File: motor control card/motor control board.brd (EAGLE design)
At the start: 100 x 80 mm, 13 parts, among them J1 8-1393644-0, J2 TBP02R1-381-07BE, J3 TBP02R1-381-07BE

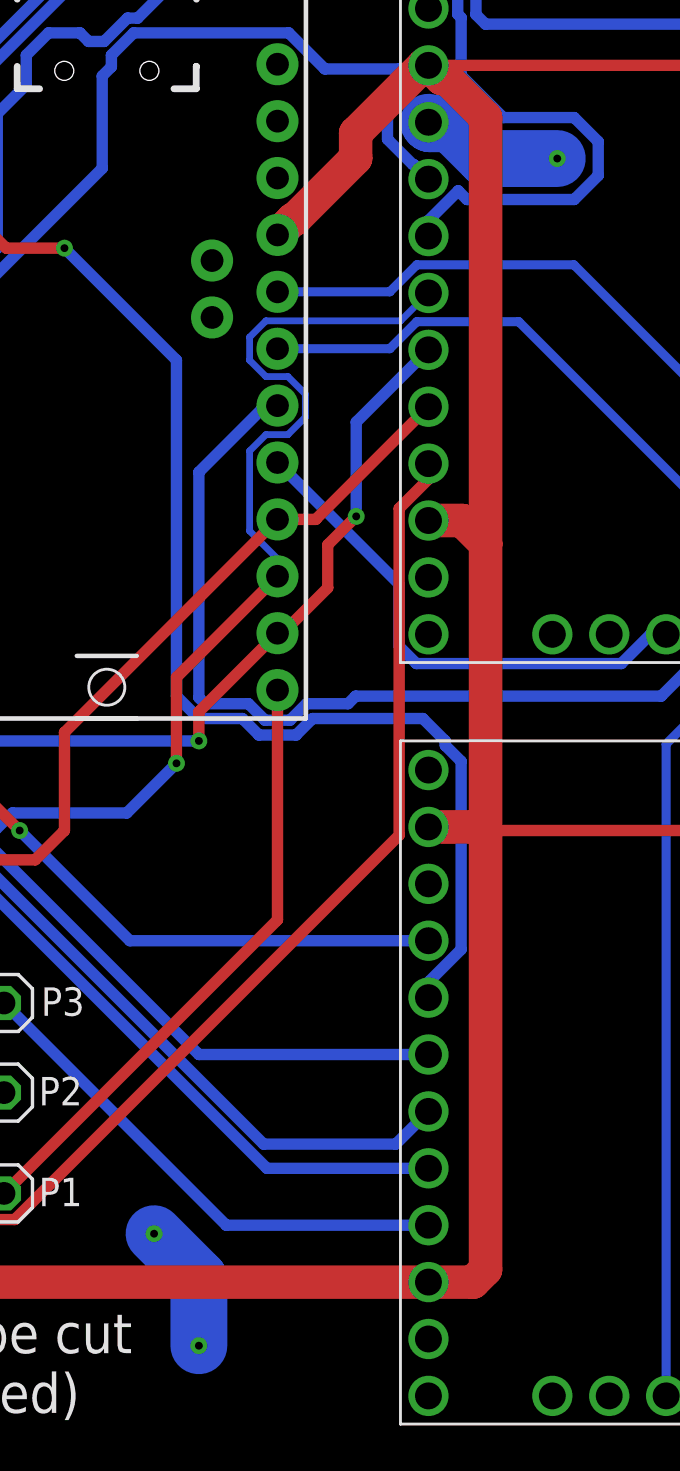
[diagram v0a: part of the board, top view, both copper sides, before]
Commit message: motor driver schematic has been verified, added the valves board, will validate it though
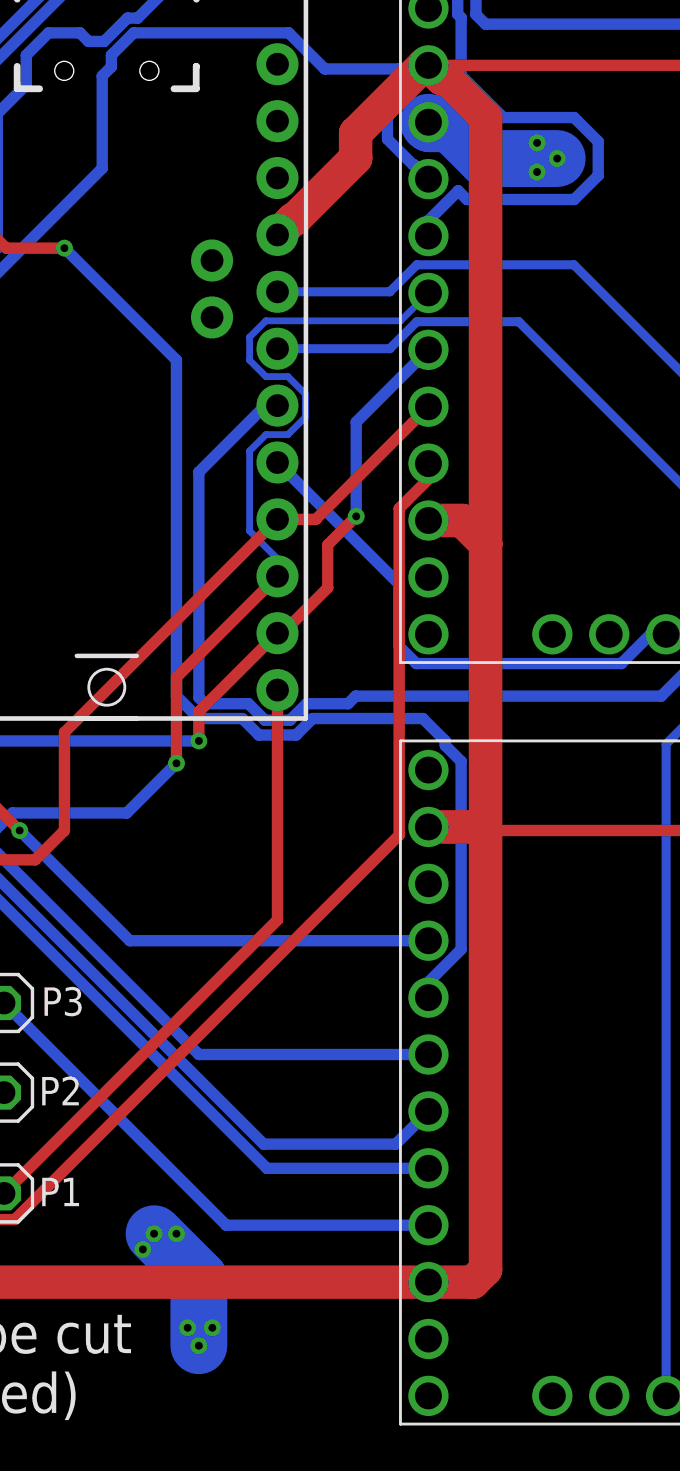
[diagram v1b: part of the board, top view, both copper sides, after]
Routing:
- net GND: vias 3 -> 9
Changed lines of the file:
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@@
 <wire x1="40" y1="19" x2="42" y2="17" width="2.54" layer="16"/>
 <wire x1="42" y1="17" x2="42" y2="14" width="2.54" layer="16"/>
+<via x="57.1" y="66.4" extent="1-16" drill="0.35"/>
+<via x="57.1" y="67.7" extent="1-16" drill="0.35"/>
+<via x="41" y="19" extent="1-16" drill="0.35"/>
+<via x="39.5" y="18.3" extent="1-16" drill="0.35"/>
+<via x="41.5" y="14.8" extent="1-16" drill="0.35"/>
+<via x="42.6" y="14.8" extent="1-16" drill="0.35"/>
 </signal>
 <signal name="24V/12V">

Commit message: fixed library attributes for the din41612 connector, fixed git problems
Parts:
- J1: value 8-1393644-0 -> 09231486921; device 8-1393644-0:TE_8-1393644-0 -> din41612_48_pin_board:HARTING_09231486921
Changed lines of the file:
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@@
 </autorouter>
 <elements>
-<element name="J1" library="8-1393644-0" package="TE_8-1393644-0" value="8-1393644-0" x="5.6" y="21" locked="yes" smashed="yes" rot="R270">
+<element name="J1" library="din41612_48_pin_board" package="HARTING_09231486921" value="09231486921" x="5.6" y="21" locked="yes" smashed="yes" rot="R270">
 <attribute name="AVAILABILITY" value="In Stock" x="5.6" y="21" locked="yes" size="1.778" layer="27" rot="R270" display="off"/>
-<attribute name="COMMENT" value="8-1393644-0" x="5.6" y="21" locked="yes" size="1.778" layer="27" rot="R270" display="off"/>
+<attribute name="COMMENT" value="09231486921" x="5.6" y="21" locked="yes" size="1.778" layer="27" rot="R270" display="off"/>
 <attribute name="DESCRIPTION" value=" Conn DIN 41612 M 48 POS 2.54mm Solder RA Thru-Hole Tray " x="5.6" y="21" locked="yes" size="1.778" layer="27" rot="R270" display="off"/>
 <attribute name="EU_ROHS_COMPLIANCE" value="Compliant" x="5.6" y="21" locked="yes" size="1.778" layer="27" rot="R270" display="off"/>
-<attribute name="MF" value="TE Connectivity" x="5.6" y="21" locked="yes" size="1.778" layer="27" rot="R270" display="off"/>
-<attribute name="MP" value="8-1393644-0" x="5.6" y="21" locked="yes" size="1.778" layer="27" rot="R270" display="off"/>
+<attribute name="MF" value="HARTING" x="5.6" y="21" locked="yes" size="1.778" layer="27" rot="R270" display="off"/>
+<attribute name="MP" value="09231486921" x="5.6" y="21" locked="yes" size="1.778" layer="27" rot="R270" display="off"/>
 <attribute name="NAME" x="7.605" y="69.73" locked="yes" size="1.27" layer="25" rot="R270"/>
 <attribute name="PACKAGE" value="None" x="5.6" y="21" locked="yes" size="1.778" layer="27" rot="R270" display="off"/>
-<attribute name="PRICE" value="None" x="5.6" y="21" locked="yes" size="1.778" layer="27" rot="R270" display="off"/>
-<attribute name="PURCHASE-URL" value="https://pricing.snapeda.com/search/part/8-1393644-0/?ref=eda" x="5.6" y="21" locked="yes" size="1.778" layer="27" rot="R270" display="off"/>
+<attribute name="PRICE" value="6$" x="5.6" y="21" locked="yes" size="1.778" layer="27" rot="R270" display="off"/>
+<attribute name="PURCHASE-URL-DIGIKEY" value="https://www.digikey.ca/en/products/detail/harting/09231486921/3180439" x="5.6" y="21" size="1.778" layer="27" rot="R270" display="off"/>
 <attribute name="VALUE" x="-8.59" y="67.73" locked="yes" size="1.27" layer="27" rot="R270"/>
 </element>
@@
 <via x="41.5" y="14.8" extent="1-16" drill="0.35"/>
 <via x="42.6" y="14.8" extent="1-16" drill="0.35"/>
+<wire x1="82.73" y1="58.49" x2="91" y2="59.24" width="0" layer="19" extent="1-1"/>
+<wire x1="82.73" y1="55.95" x2="82.73" y2="58.49" width="0" layer="19" extent="1-1"/>
+<wire x1="58" y1="67" x2="82.73" y2="58.49" width="0" layer="19" extent="1-1"/>
+<wire x1="57.1" y1="66.4" x2="58" y2="67" width="0" layer="19" extent="1-1"/>
+<wire x1="57.1" y1="67.7" x2="58" y2="67" width="0" layer="19" extent="1-1"/>
+<wire x1="30.27" y1="50.89" x2="52.25" y2="68.62" width="0" layer="19" extent="1-1"/>
+<wire x1="52.25" y1="34.62" x2="30.27" y2="50.89" width="0" layer="19" extent="1-1"/>
+<wire x1="41" y1="19" x2="52.25" y2="34.62" width="0" layer="19" extent="1-1"/>
+<wire x1="40" y1="19" x2="41" y2="19" width="0" layer="19" extent="1-1"/>
+<wire x1="39.5" y1="18.3" x2="40" y2="19" width="0" layer="19" extent="1-1"/>
+<wire x1="41.5" y1="14.8" x2="42" y2="14" width="0" layer="19" extent="1-1"/>
+<wire x1="42.6" y1="14.8" x2="42" y2="14" width="0" layer="19" extent="1-1"/>
+<wire x1="10.68" y1="21" x2="39.5" y2="18.3" width="0" layer="19" extent="1-1"/>
+<wire x1="10.68" y1="23.54" x2="10.68" y2="21" width="0" layer="19" extent="1-1"/>
+<wire x1="10.68" y1="26.08" x2="10.68" y2="23.54" width="0" layer="19" extent="1-1"/>
+<wire x1="8.14" y1="26.08" x2="10.68" y2="26.08" width="0" layer="19" extent="1-1"/>
+<wire x1="5.6" y1="26.08" x2="8.14" y2="26.08" width="0" layer="19" extent="1-1"/>
+<wire x1="5.6" y1="28.62" x2="5.6" y2="26.08" width="0" layer="19" extent="1-1"/>
+<wire x1="8.14" y1="23.54" x2="10.68" y2="23.54" width="0" layer="19" extent="1-1"/>
+<wire x1="5.6" y1="23.54" x2="5.6" y2="26.08" width="0" layer="19" extent="1-1"/>
+<wire x1="8.14" y1="21" x2="10.68" y2="21" width="0" layer="19" extent="1-1"/>
+<wire x1="5.6" y1="21" x2="5.6" y2="23.54" width="0" layer="19" extent="1-1"/>
+<wire x1="91" y1="27.38" x2="82.73" y2="55.95" width="0" layer="19" extent="1-1"/>
+<wire x1="82.73" y1="24.49" x2="91" y2="27.38" width="0" layer="19" extent="1-1"/>
+<wire x1="82.73" y1="21.95" x2="82.73" y2="24.49" width="0" layer="19" extent="1-1"/>
 </signal>
 <signal name="24V/12V">
@@
 <vertex x="5.1" y="33.8"/>
 </polygon>
+<wire x1="82.73" y1="50.87" x2="82.73" y2="53.41" width="0" layer="19" extent="1-1"/>
+<wire x1="82.73" y1="19.41" x2="82.73" y2="50.87" width="0" layer="19" extent="1-1"/>
+<wire x1="82.73" y1="16.87" x2="82.73" y2="19.41" width="0" layer="19" extent="1-1"/>
+<wire x1="10.68" y1="28.62" x2="82.73" y2="19.41" width="0" layer="19" extent="1-1"/>
+<wire x1="10.68" y1="31.16" x2="10.68" y2="28.62" width="0" layer="19" extent="1-1"/>
+<wire x1="8.14" y1="31.16" x2="10.68" y2="31.16" width="0" layer="19" extent="1-1"/>
+<wire x1="8.14" y1="33.7" x2="8.14" y2="31.16" width="0" layer="19" extent="1-1"/>
+<wire x1="5.6" y1="33.7" x2="8.14" y2="33.7" width="0" layer="19" extent="1-1"/>
+<wire x1="5.6" y1="31.16" x2="8.14" y2="31.16" width="0" layer="19" extent="1-1"/>
+<wire x1="8.14" y1="28.62" x2="10.68" y2="28.62" width="0" layer="19" extent="1-1"/>
 </signal>
 <signal name="5V">

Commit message: added cam data
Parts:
- U$1, U$2: device high power stepper driver 36V4:BREAKOUT_BOARD -> high_power_stepper_driver_36V4:BREAKOUT_BOARD
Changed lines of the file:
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@@
 <attribute name="VALUE" x="-8.59" y="67.73" locked="yes" size="1.27" layer="27" rot="R270"/>
 </element>
-<element name="U$1" library="high power stepper driver 36V4" package="BREAKOUT_BOARD" value="POLOLU_HIGH-POWER_STEPPER_MOTOR_DRIVER_36V4" x="84" y="75" locked="yes" smashed="yes" rot="R180"/>
-<element name="U$3" library="SparkFun-SAMD21-Mini-Breakout" package="JP1_SPARKFUN-SAMD21-MINI-BREAKOUT-V10" value="" x="29" y="42" locked="yes" smashed="yes"/>
-<element name="U$2" library="high power stepper driver 36V4" package="BREAKOUT_BOARD" value="POLOLU_HIGH-POWER_STEPPER_MOTOR_DRIVER_36V4" x="84" y="41" smashed="yes" rot="R180"/>
+<element name="U$1" library="high_power_stepper_driver_36V4" package="BREAKOUT_BOARD" value="POLOLU_HIGH-POWER_STEPPER_MOTOR_DRIVER_36V4" x="84" y="75" locked="yes" smashed="yes" rot="R180">
+<attribute name="PURCHASE_URL_POLOLU" value="https://www.pololu.com/product/3730/resources" x="84" y="75" size="1.778" layer="27" rot="R180" display="off"/>
+</element>
+<element name="U$3" library="SparkFun-SAMD21-Mini-Breakout" package="JP1_SPARKFUN-SAMD21-MINI-BREAKOUT-V10" value="" x="29" y="42" locked="yes" smashed="yes">
+<attribute name="PURCHASE_URL_DIGIKEY" value="https://www.digikey.ca/en/products/detail/sparkfun-electronics/DEV-13664/5766914?s=N4IgTCBcDaIM4EMC2ATMBGABEglgOx0wCMAnAUwQGsB7AVwBcQBdAXyA" x="29" y="42" size="1.778" layer="27" display="off"/>
+<attribute name="PURCHASE_URL_SPARKFUN" value="https://www.sparkfun.com/products/13664" x="29" y="42" size="1.778" layer="27" display="off"/>
+</element>
+<element name="U$2" library="high_power_stepper_driver_36V4" package="BREAKOUT_BOARD" value="POLOLU_HIGH-POWER_STEPPER_MOTOR_DRIVER_36V4" x="84" y="41" smashed="yes" rot="R180">
+<attribute name="PURCHASE_URL_POLOLU" value="https://www.pololu.com/product/3730/resources" x="84" y="41" size="1.778" layer="27" rot="R180" display="off"/>
+</element>
 <element name="J2" library="TBP02R1-381-07BE" package="CUI_TBP02R1-381-07BE" value="TBP02R1-381-07BE" x="91" y="35" locked="yes" smashed="yes" rot="R270">
 <attribute name="AVAILABILITY" value="In Stock" x="91" y="36" locked="yes" size="1.778" layer="27" rot="R270" display="off"/>
@@
 <contactref element="J1" pad="19"/>
 <contactref element="J1" pad="18"/>
-<contactref element="U$3" pad="4@JP1"/>
 <contactref element="J2" pad="3"/>
 <contactref element="J3" pad="3"/>
@@
 <via x="41.5" y="14.8" extent="1-16" drill="0.35"/>
 <via x="42.6" y="14.8" extent="1-16" drill="0.35"/>
-<wire x1="82.73" y1="58.49" x2="91" y2="59.24" width="0" layer="19" extent="1-1"/>
-<wire x1="82.73" y1="55.95" x2="82.73" y2="58.49" width="0" layer="19" extent="1-1"/>
-<wire x1="58" y1="67" x2="82.73" y2="58.49" width="0" layer="19" extent="1-1"/>
-<wire x1="57.1" y1="66.4" x2="58" y2="67" width="0" layer="19" extent="1-1"/>
-<wire x1="57.1" y1="67.7" x2="58" y2="67" width="0" layer="19" extent="1-1"/>
-<wire x1="30.27" y1="50.89" x2="52.25" y2="68.62" width="0" layer="19" extent="1-1"/>
-<wire x1="52.25" y1="34.62" x2="30.27" y2="50.89" width="0" layer="19" extent="1-1"/>
-<wire x1="41" y1="19" x2="52.25" y2="34.62" width="0" layer="19" extent="1-1"/>
-<wire x1="40" y1="19" x2="41" y2="19" width="0" layer="19" extent="1-1"/>
-<wire x1="39.5" y1="18.3" x2="40" y2="19" width="0" layer="19" extent="1-1"/>
-<wire x1="41.5" y1="14.8" x2="42" y2="14" width="0" layer="19" extent="1-1"/>
-<wire x1="42.6" y1="14.8" x2="42" y2="14" width="0" layer="19" extent="1-1"/>
-<wire x1="10.68" y1="21" x2="39.5" y2="18.3" width="0" layer="19" extent="1-1"/>
-<wire x1="10.68" y1="23.54" x2="10.68" y2="21" width="0" layer="19" extent="1-1"/>
-<wire x1="10.68" y1="26.08" x2="10.68" y2="23.54" width="0" layer="19" extent="1-1"/>
-<wire x1="8.14" y1="26.08" x2="10.68" y2="26.08" width="0" layer="19" extent="1-1"/>
-<wire x1="5.6" y1="26.08" x2="8.14" y2="26.08" width="0" layer="19" extent="1-1"/>
-<wire x1="5.6" y1="28.62" x2="5.6" y2="26.08" width="0" layer="19" extent="1-1"/>
-<wire x1="8.14" y1="23.54" x2="10.68" y2="23.54" width="0" layer="19" extent="1-1"/>
-<wire x1="5.6" y1="23.54" x2="5.6" y2="26.08" width="0" layer="19" extent="1-1"/>
-<wire x1="8.14" y1="21" x2="10.68" y2="21" width="0" layer="19" extent="1-1"/>
-<wire x1="5.6" y1="21" x2="5.6" y2="23.54" width="0" layer="19" extent="1-1"/>
-<wire x1="91" y1="27.38" x2="82.73" y2="55.95" width="0" layer="19" extent="1-1"/>
-<wire x1="82.73" y1="24.49" x2="91" y2="27.38" width="0" layer="19" extent="1-1"/>
-<wire x1="82.73" y1="21.95" x2="82.73" y2="24.49" width="0" layer="19" extent="1-1"/>
+<contactref element="U$3" pad="4@JP1"/>
 </signal>
 <signal name="24V/12V">
@@
 <vertex x="5.1" y="33.8"/>
 </polygon>
-<wire x1="82.73" y1="50.87" x2="82.73" y2="53.41" width="0" layer="19" extent="1-1"/>
-<wire x1="82.73" y1="19.41" x2="82.73" y2="50.87" width="0" layer="19" extent="1-1"/>
-<wire x1="82.73" y1="16.87" x2="82.73" y2="19.41" width="0" layer="19" extent="1-1"/>
-<wire x1="10.68" y1="28.62" x2="82.73" y2="19.41" width="0" layer="19" extent="1-1"/>
-<wire x1="10.68" y1="31.16" x2="10.68" y2="28.62" width="0" layer="19" extent="1-1"/>
-<wire x1="8.14" y1="31.16" x2="10.68" y2="31.16" width="0" layer="19" extent="1-1"/>
-<wire x1="8.14" y1="33.7" x2="8.14" y2="31.16" width="0" layer="19" extent="1-1"/>
-<wire x1="5.6" y1="33.7" x2="8.14" y2="33.7" width="0" layer="19" extent="1-1"/>
-<wire x1="5.6" y1="31.16" x2="8.14" y2="31.16" width="0" layer="19" extent="1-1"/>
-<wire x1="8.14" y1="28.62" x2="10.68" y2="28.62" width="0" layer="19" extent="1-1"/>
 </signal>
 <signal name="5V">
@@
 <mfgpreviewcolor name="substratecolor" color="0xFF786E46"/>
 </mfgpreviewcolors>
+<errors>
+</errors>
 </board>
 </drawing>
